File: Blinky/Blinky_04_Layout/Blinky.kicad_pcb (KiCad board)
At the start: 2 copper layers, 29 x 29 mm, 12 parts, among them SW1 SW_SPDT, U1 NE555

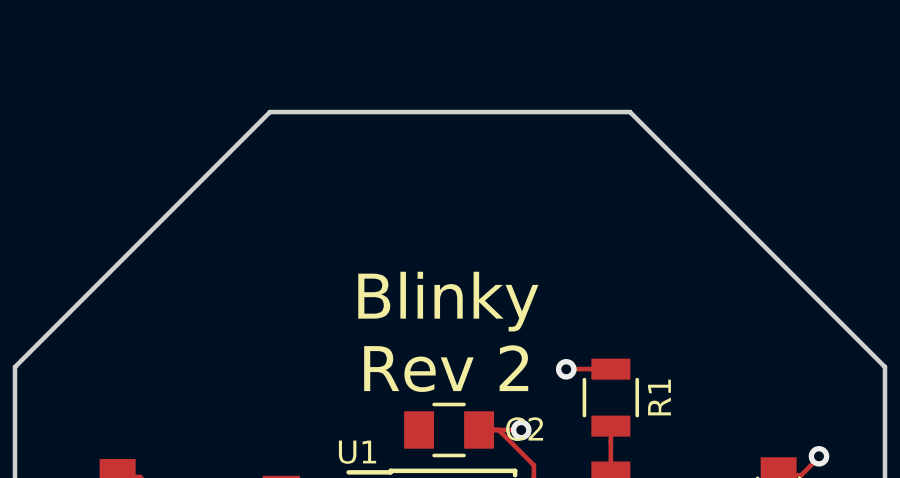
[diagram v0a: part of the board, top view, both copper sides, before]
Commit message: Added the mounting hole that was removed during the cleanup
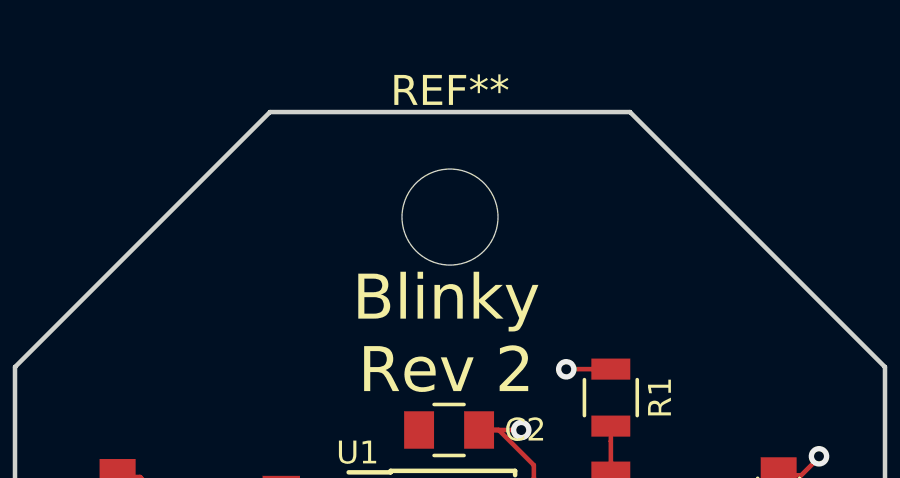
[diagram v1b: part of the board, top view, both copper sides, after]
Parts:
- added REF**: MountingHole_3.2mm_M3, Mounting_Holes:MountingHole_3.2mm_M3, F.Cu at (69.5, 78.5)
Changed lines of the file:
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@@
     (tracks 58)
     (zones 0)
-    (modules 12)
+    (modules 13)
     (nets 11)
   )
@@
     )
   )
+  (module Mounting_Holes:MountingHole_3.2mm_M3 (layer F.Cu)
+    (at 69.5 78.5)
+    (descr "Mounting Hole 3.2mm, no annular, M3")
+    (tags "mounting hole 3.2mm no annular m3")
+    (attr virtual)
+    (fp_text reference REF** (at 0 -4.2) (layer F.SilkS)
+      (effects (font (size 1 1) (thickness 0.15)))
+    )
+    (fp_text value MountingHole_3.2mm_M3 (at 0 4.2) (layer F.Fab)
+      (effects (font (size 1 1) (thickness 0.15)))
+    )
+    (fp_text user %R (at 0.3 0) (layer F.Fab)
+      (effects (font (size 1 1) (thickness 0.15)))
+    )
+    (fp_circle (center 0 0) (end 3.2 0) (layer Cmts.User) (width 0.15))
+    (fp_circle (center 0 0) (end 3.45 0) (layer F.CrtYd) (width 0.05))
+    (pad 1 np_thru_hole circle (at 0 0) (size 3.2 3.2) (drill 3.2) (layers *.Cu *.Mask))
+  )
   (gr_line (start 55 83.5) (end 63.5 75) (layer Edge.Cuts) (width 0.15))

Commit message: Baseline ...
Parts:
- removed C3: 300n, Capacitors_SMD:C_0805
- removed REF***: KiCad-Logo2_6mm_SilkScreen, Symbols:KiCad-Logo2_6mm_SilkScreen
- added C1: 300n, Capacitor_SMD:C_0805_2012Metric, F.Cu at (64.0, 89.6)
- added REF**: KiCad-Logo2_6mm_SilkScreen, Symbol:KiCad-Logo2_6mm_SilkScreen, F.Cu at (69.4, 100.0)
- C2: footprint Capacitors_SMD:C_0805 -> Capacitor_SMD:C_0805_2012Metric
- D1, D2: footprint LEDs:LED_0805 -> LED_SMD:LED_0805_2012Metric
- R1, R4: footprint Resistors_SMD:R_0805 -> Resistor_SMD:R_0805_2012Metric
- R2: value 200 -> 1M; footprint Resistors_SMD:R_0805 -> Resistor_SMD:R_0805_2012Metric
- R3: value 1M -> 200; footprint Resistors_SMD:R_0805 -> Resistor_SMD:R_0805_2012Metric
- SW1: footprint Blinky:Micro_Schiebeschalter -> Button_Switch_SMD:SW_SPDT_PCM12
- U1: footprint Housings_SOIC:SOIC-8_3.9x4.9mm_Pitch1.27mm -> Package_SO:SOIC-8_3.9x4.9mm_P1.27mm
- moved R4 21.4 mm to (79.3, 88.0), turned to 90 degrees
- moved D2 21.2 mm to (79.3, 91.7), turned to 270 degrees
- moved D1 21.1 mm to (59.7, 92.1), turned to 270 degrees
- moved R3 15.2 mm to (59.7, 88.1), turned to 90 degrees
- moved R2 6.13 mm to (74.4, 91.6)
- moved R1 3.21 mm to (74.4, 87.7)
- moved SW1 1.62 mm to (69.6, 100.5), turned to 180 degrees
- moved U1 1.11 mm to (69.3, 90.6)
- moved C2 1.01 mm to (69.6, 86.6)
- moved BT1 0.99 mm to (69.5, 90.4)
- renumbered REF** to ?
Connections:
- R2 pad 1: Net-(D1-Pad1) -> Net-(R1-Pad2)
- R2 pad 2: Net-(D2-Pad2) -> Net-(C1-Pad1)
- R3 pad 1: Net-(R1-Pad2) -> Net-(D1-Pad1)
- R3 pad 2: Net-(C3-Pad1) -> Net-(D2-Pad2)
- U1 pad 2: Net-(C3-Pad1) -> Net-(C1-Pad1)
- U1 pad 6: Net-(C3-Pad1) -> Net-(C1-Pad1)
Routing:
- net Net-(C3-Pad1): track 13.0 -> 0.00 mm
- net Net-(C1-Pad1): track 0.00 -> 11.7 mm
- net /Vcc: track 8.98 -> 12.0 mm
- net Net-(D2-Pad2): track 25.4 -> 23.1 mm
- net Net-(BT1-Pad1): track 25.3 -> 23.2 mm
- net GND: track 2.64 -> 2.98 mm, vias 1 -> 2
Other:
- board text removed: "Blinky Rev 2"
